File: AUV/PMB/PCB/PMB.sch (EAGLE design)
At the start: 95 parts, among them Q1 CRYSTAL_SM49, SW1 MC32829, U6 ATMEGA328P-AU, X1 16MHz

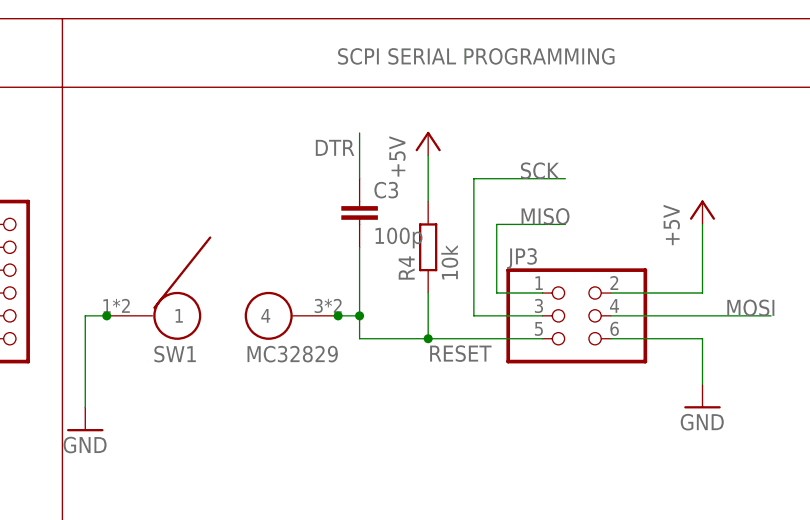
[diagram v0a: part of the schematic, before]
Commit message: Shifted libraries to same folder as main code. Calibration files updated for PMB1,2,3,4,5,6.
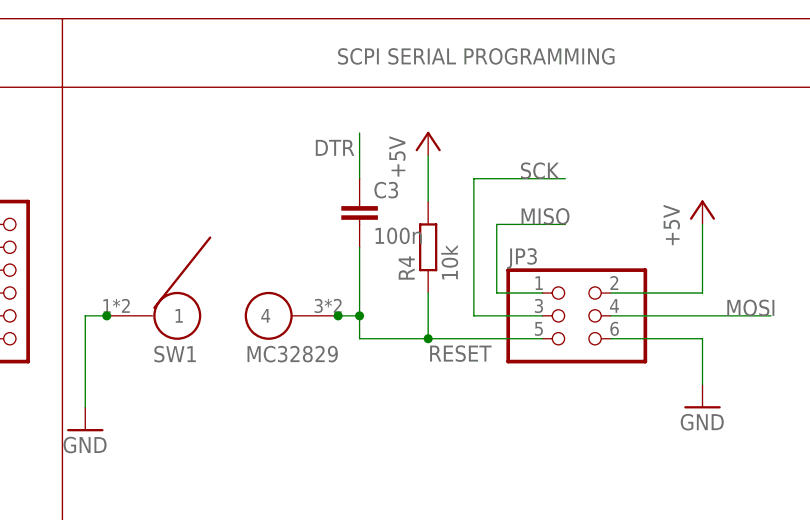
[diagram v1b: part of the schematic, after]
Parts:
- C3: value 100p -> 100n
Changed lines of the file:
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@@
 <?xml version="1.0" encoding="utf-8"?>
 <!DOCTYPE eagle SYSTEM "eagle.dtd">
-<eagle version="6.6.0">
+<eagle version="8.1.0">
 <drawing>
 <settings>
@@
 <part name="SW1" library="mc32829(pb_sw)" deviceset="MC32829" device=""/>
 <part name="GND7" library="supply1" deviceset="GND" device=""/>
-<part name="C3" library="SparkFun-Capacitors" deviceset="CAP" device="0805" value="100p"/>
+<part name="C3" library="SparkFun-Capacitors" deviceset="CAP" device="0805" value="100n"/>
 <part name="R4" library="resistor" deviceset="R-EU_" device="R0805W" value="10k"/>
 <part name="P+8" library="supply1" deviceset="+5V" device=""/>
